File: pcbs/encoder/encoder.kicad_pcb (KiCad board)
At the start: 2 copper layers, 28 x 29.7 mm, 10 parts, among them P1 M1, P2 M2, P3 Motor, P4 CONN_01X04, U1 TCRT1000, U2 TCRT1000

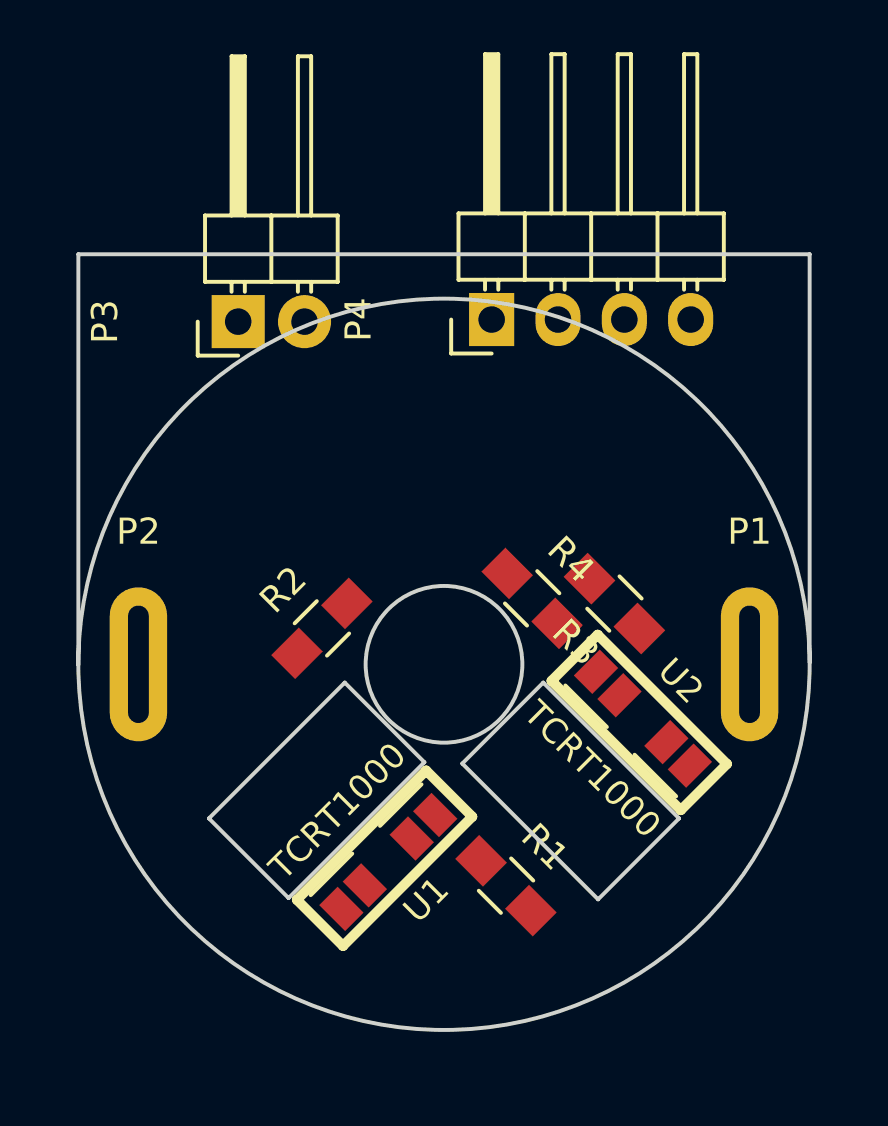
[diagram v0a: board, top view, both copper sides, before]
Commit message: pcb del encoder
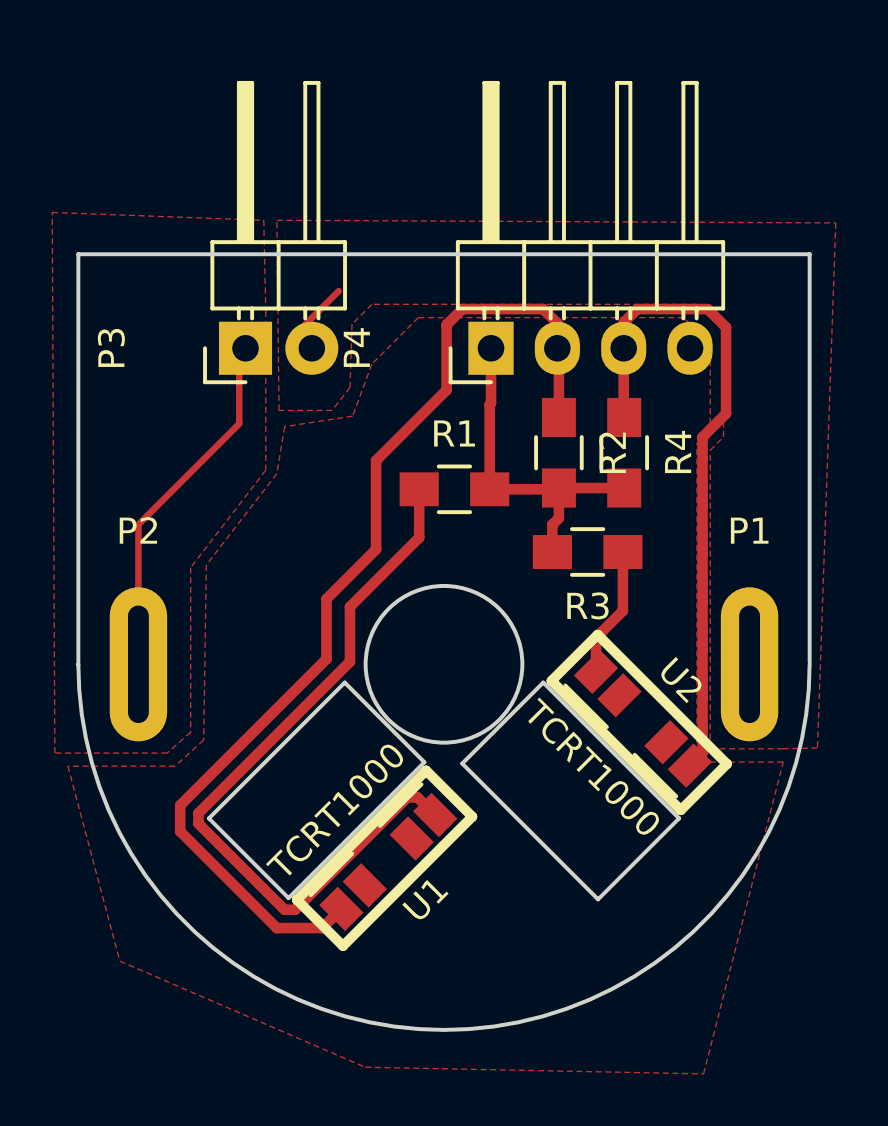
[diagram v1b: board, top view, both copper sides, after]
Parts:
- moved R1 15.3 mm to (145.4, 100.3), turned to 0 degrees
- moved R2 11.3 mm to (149.4, 98.9), turned to 270 degrees
- moved R4 6.60 mm to (151.9, 98.9), turned to 270 degrees
- moved R3 2.23 mm to (150.5, 102.7), turned to 180 degrees
- moved P4 1.10 mm to (146.8, 94.9)
- moved P3 1.06 mm to (137.4, 94.9)
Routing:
- net /S1: track 0.00 -> 40.9 mm
- net Net-(R1-Pad1): track 0.00 -> 28.8 mm
- net /S2: track 0.00 -> 25.4 mm
- net Net-(P2-Pad1): track 0.00 -> 13.3 mm
- net +5V: track 0.00 -> 13.1 mm
- net Net-(R3-Pad1): track 0.00 -> 5.01 mm
- net Net-(P1-Pad1): track 0.00 -> 3.07 mm
- added copper zone on F.Cu, net GND
- added copper zone on F.Cu, net Net-(P1-Pad1)
- added copper zone on F.Cu, net Net-(P2-Pad1)
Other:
- outline, holes or cut-outs redrawn
- net class Default: clearance 0.2 -> 0.254; trace_width 0.25 -> 0.3048
- rule trace_clearance: 0.2 -> 0.254
